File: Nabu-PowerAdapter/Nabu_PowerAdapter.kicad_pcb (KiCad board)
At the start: 2 copper layers, 28.4 x 37.6 mm, 6 parts, among them J1 Conn_01x06_Male, J2 MB, J3 MB, J4 MB, J5 Fan

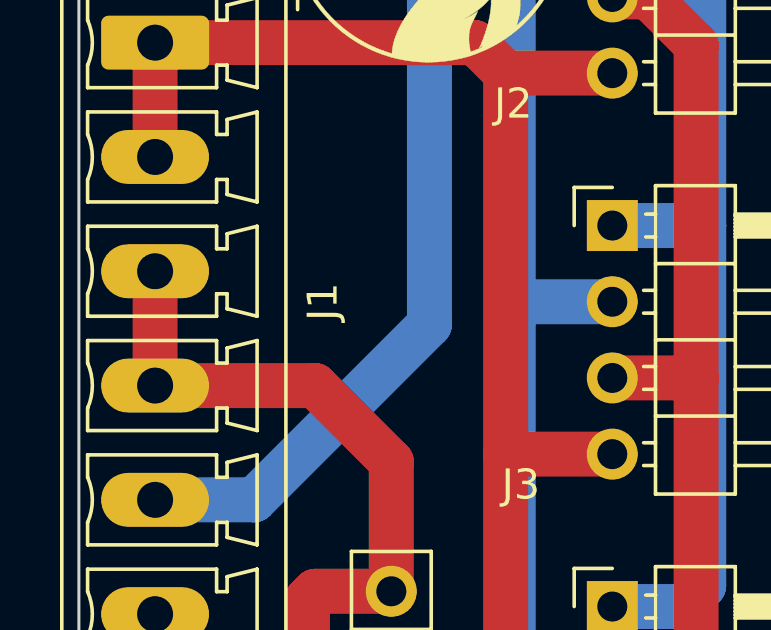
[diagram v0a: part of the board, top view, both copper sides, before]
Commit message: Add power labels and upgrade project to KiCAD 7.0.1
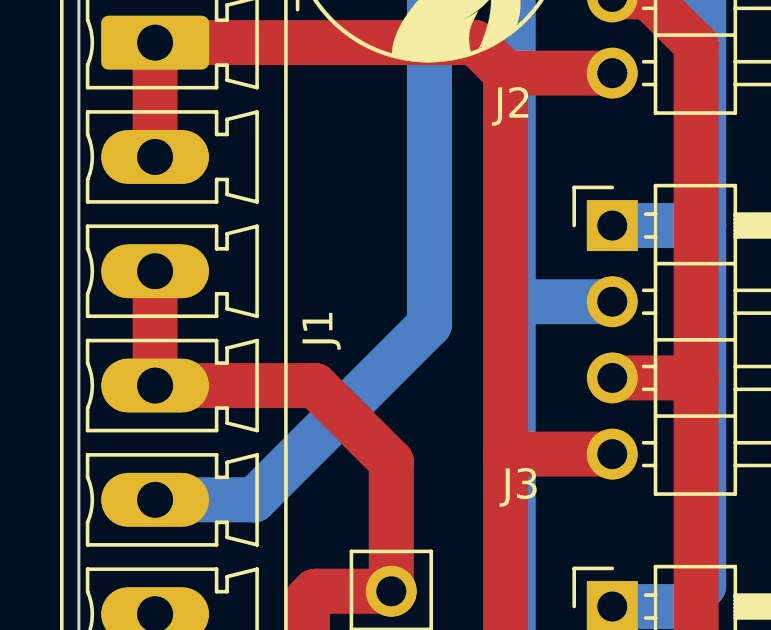
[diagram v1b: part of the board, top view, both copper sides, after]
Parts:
- J1: value Conn_01x06_Male -> Conn_01x06
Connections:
- net Net-(J1-Pad1) renamed +5V
- net Net-(J1-Pad3) renamed GND
- net Net-(J1-Pad5) renamed -12V
- net Net-(J1-Pad6) renamed +12V
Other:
- net class Default removed
